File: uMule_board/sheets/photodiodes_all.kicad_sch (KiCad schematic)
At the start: 0 parts

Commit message: Started working on PCB. Ditched high power outputs. Focusing on photodiodes. One commit closer to order
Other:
- title: (none) -> uMule_board
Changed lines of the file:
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@@
 	(generator_version "9.0")
 	(paper "A4")
+	(title_block
+		(title "uMule_board")
+		(date "2025-12-14")
+		(rev "1.0")
+		(comment 1 "Original author: Oliwier Woźniak")
+	)
 	(bus_entry
 		(at 120.65 86.36)
@@
 	)
 	(sheet
-		(at 83.82 46.99)
-		(size 12.7 5.08)
-		(exclude_from_sim no)
-		(in_bom yes)
-		(on_board yes)
-		(dnp no)
-		(fields_autoplaced yes)
-		(stroke
-			(width 0.1524)
-			(type solid)
-		)
-		(fill
-			(color 0 0 0 0.0000)
-		)
-		(property "Sheetname" "Photodiode1"
-			(at 83.82 46.2784 0)
-			(effects
-				(font
-					(size 1.27 1.27)
-				)
-				(justify left bottom)
-			)
-		)
-		(property "Sheetfile" "photodiode.kicad_sch"
-			(at 83.82 52.6546 0)
-			(effects
-				(font
-					(size 1.27 1.27)
-				)
-				(justify left top)
-			)
-		)
-		(pin "SIGNAL" output
-			(at 83.82 49.53 180)
-			(effects
-				(font
-					(size 1.27 1.27)
-				)
-				(justify left)
-			)
-		)
-		(instances
-			(project "uMule_board"
-				(path "/3d853824-a92e-40a5-ad1a-5052c8a0bd68/6627633c-9ae5-4253-9ddc-73b5516d7e53"
-					(page "5")
-				)
-			)
-		)
-	)
-	(sheet
 		(at 133.35 35.56)
 		(size 12.7 5.08)
@@
 				)
 			)
+		)
+	)
+	(sheet
+		(at 83.82 46.99)
+		(size 12.7 5.08)
+		(exclude_from_sim no)
+		(in_bom yes)
+		(on_board yes)
+		(dnp no)
+		(fields_autoplaced yes)
+		(stroke
+			(width 0.1524)
+			(type solid)
+		)
+		(fill
+			(color 0 0 0 0.0000)
+		)
+		(property "Sheetname" "Photodiode1"
+			(at 83.82 46.2784 0)
+			(effects
+				(font
+					(size 1.27 1.27)
+				)
+				(justify left bottom)
+			)
+		)
+		(property "Sheetfile" "photodiode.kicad_sch"
+			(at 83.82 52.6546 0)
+			(effects
+				(font
+					(size 1.27 1.27)
+				)
+				(justify left top)
+			)
+		)
+		(pin "SIGNAL" output
+			(at 83.82 49.53 180)
+			(effects
+				(font
+					(size 1.27 1.27)
+				)
+				(justify left)
+			)
+		)
+		(instances
+			(project "uMule_board"
+				(path "/3d853824-a92e-40a5-ad1a-5052c8a0bd68/6627633c-9ae5-4253-9ddc-73b5516d7e53"
+					(page "5")
+				)
+			)

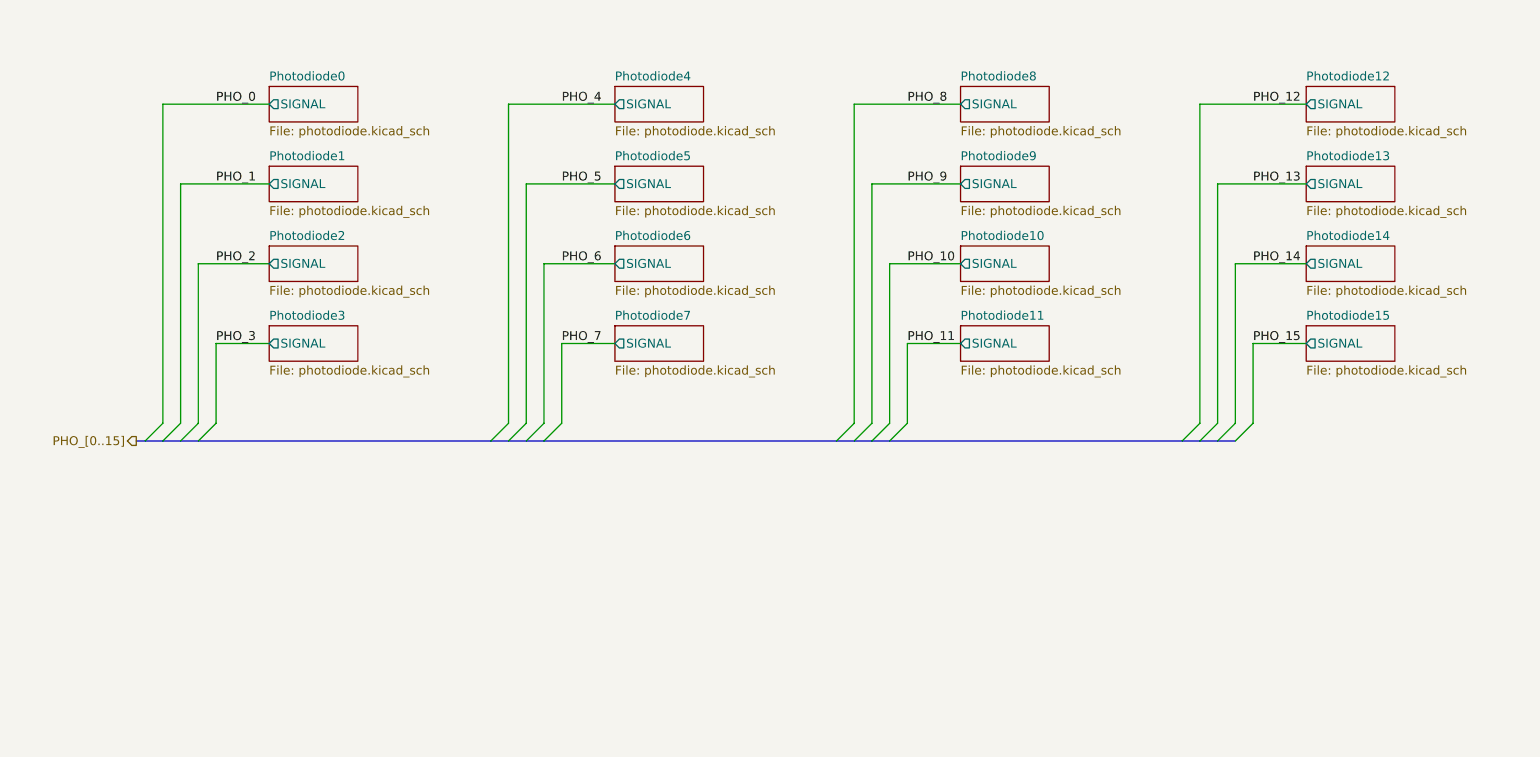
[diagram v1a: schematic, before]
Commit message: removed half phototransistors, etc.
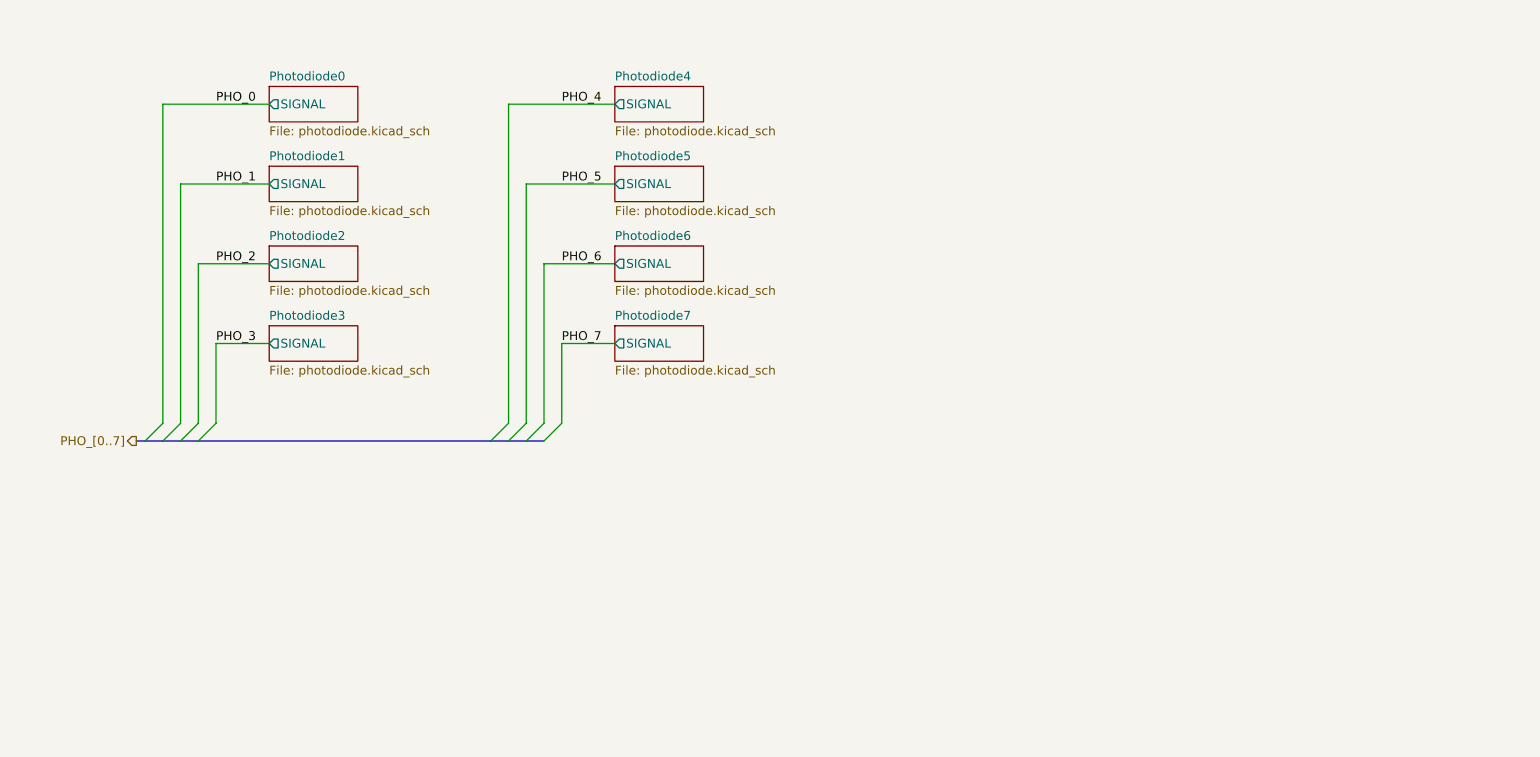
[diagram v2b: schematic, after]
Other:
- removed sheet Photodiode10
- removed sheet Photodiode11
- removed sheet Photodiode12
- removed sheet Photodiode13
- removed sheet Photodiode14
- removed sheet Photodiode15
- removed sheet Photodiode8
- removed sheet Photodiode9

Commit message: sch ready, only missing the pcb
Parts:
- added C49: 1u, Capacitor_SMD:C_0805_2012Metric_Pad1.18x1.45mm_HandSolder, symbol Device:C
- added R35: 13.7k, Resistor_SMD:R_0603_1608Metric_Pad0.98x0.95mm_HandSolder, symbol Device:R
- added R36: 280, Resistor_SMD:R_0603_1608Metric_Pad0.98x0.95mm_HandSolder, symbol Device:R
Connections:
- new net +5V: R35.2
- new net GND: C49.2, R36.1
- new net V_REF: C49.1, R35.1, R36.2
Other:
- sheet Photodiode0 ports: added V_{REF}; removed none
- sheet Photodiode1 ports: added V_{REF}; removed none
- sheet Photodiode2 ports: added V_{REF}; removed none
- sheet Photodiode3 ports: added V_{REF}; removed none
- sheet Photodiode4 ports: added V_{REF}; removed none
- sheet Photodiode5 ports: added V_{REF}; removed none
- sheet Photodiode6 ports: added V_{REF}; removed none
- sheet Photodiode7 ports: added V_{REF}; removed none
